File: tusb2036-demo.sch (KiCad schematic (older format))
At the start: 48 parts, among them J1 USB_B_Micro, J2 USB_A, J3 USB_A, J4 USB_A, SW1 RESET, U1 TUSB2036, U2 TPS76333, U3 TPS2044D, U4 SN75240, U5 SN75240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

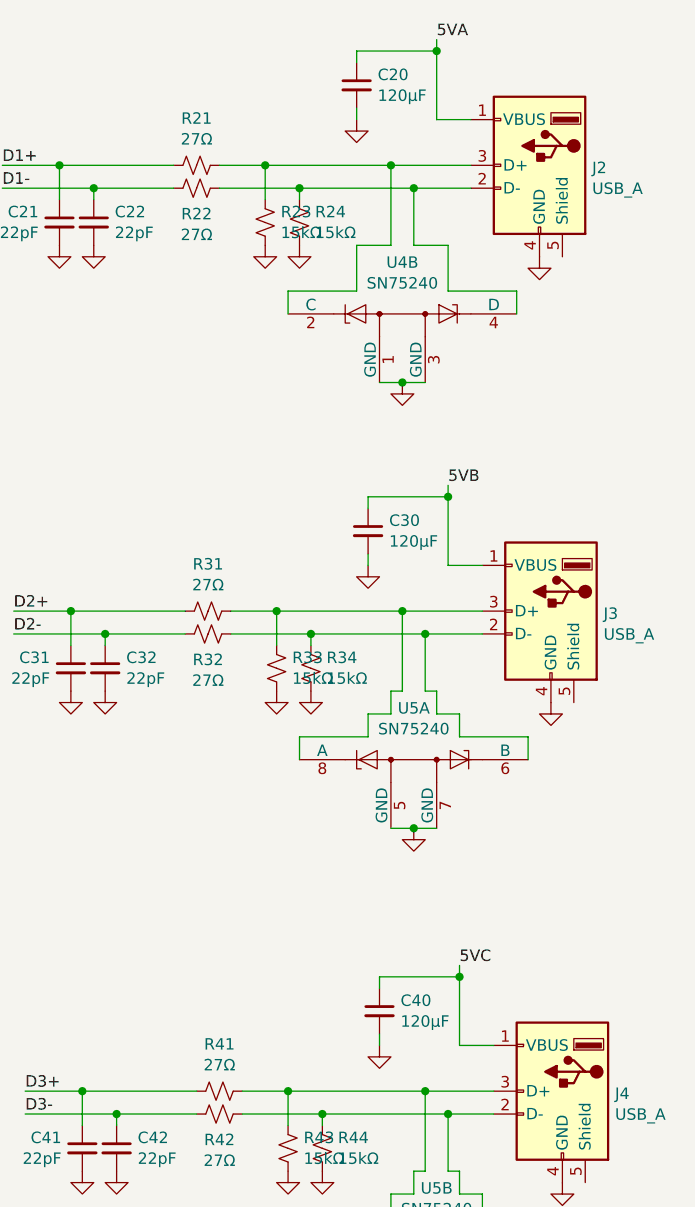
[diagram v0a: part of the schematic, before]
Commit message: Fix 120uF caps
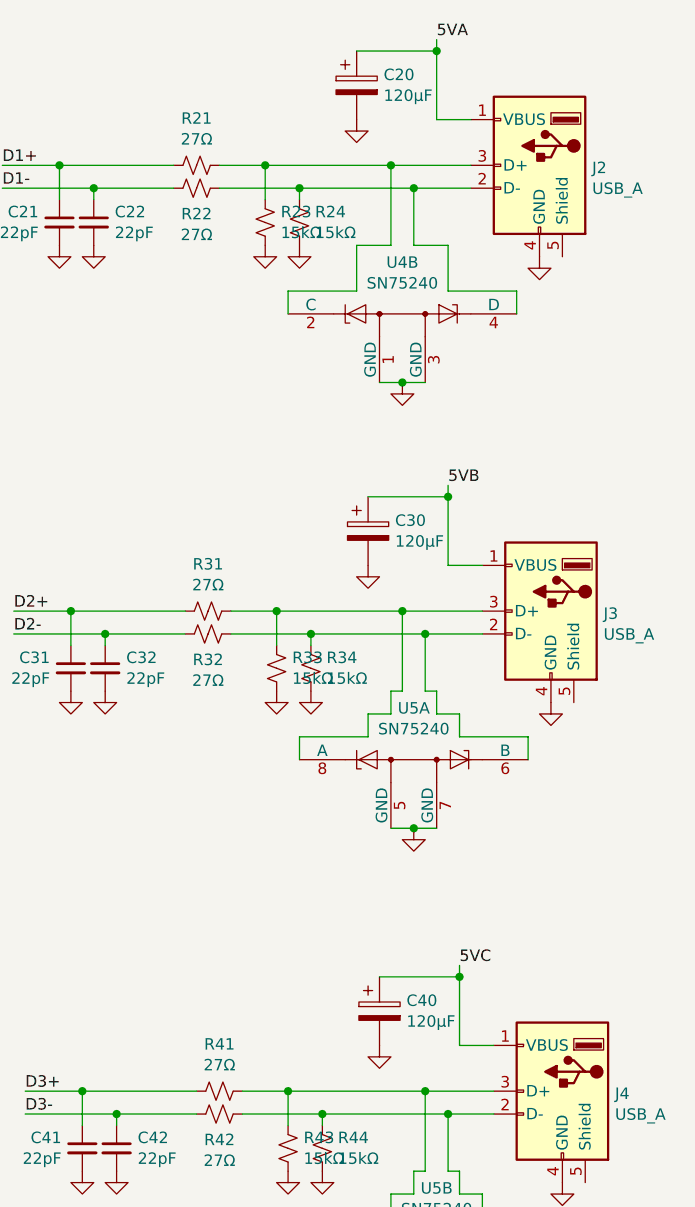
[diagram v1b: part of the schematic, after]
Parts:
- removed C20, C30, C40: 120μF, Capacitor_SMD:C_1206_3216Metric, symbol Device:C_Small
- added C20, C30, C40: 120μF, Vishay-cap:CAPPM7343X310N, symbol Device:CP
- C1, C10, C11, C2, C21, C22, C31, C32, C41, C42: Price (none) -> 0.61; Vendor (none) -> Mouser; Vendor Part # (none) -> 710-885012009007
- C3, C5: Price (none) -> 0.93; Vendor (none) -> Mouser; Vendor Part # (none) -> 80-C1210C475J3N
- C4: Price (none) -> 0.46; Vendor (none) -> Mouser; Vendor Part # (none) -> 581-12105C104JAT2A
- J3, J4: Price (none) -> 2.36; Vendor (none) -> Mouser; Vendor Part # (none) -> 710-62900416021
- JP1, JP2, JP3, JP4: Price (none) -> 0.1; Vendor (none) -> Mouser; Vendor Part # (none) -> 649-1012937890301BLF
- R1, R10, R11, R21, R22, R31, R32, R41, R42: Price (none) -> 0.14; Vendor (none) -> Mouser; Vendor Part # (none) -> 603-RC1210FR-0727RL
- R2: Price (none) -> 0.14; Vendor (none) -> Mouser; Vendor Part # (none) -> 603-RC1210FR-071K5L
- R23, R24, R33, R34, R43, R44: Price (none) -> 0.16; Vendor (none) -> Mouser; Vendor Part # (none) -> 603-RC1210FR-0715KL
- SW1: Price (none) -> 0.58; Vendor (none) -> Mouser; Vendor Part # (none) -> 653-B3FS-1002P
- TP1: Price (none) -> 0; Vendor (none) -> -; Vendor Part # (none) -> -
- U1: Price 3.40 -> 3.4
- U2: Price 1.00 -> 1
- U3: Price (none) -> 2.73; Vendor (none) -> Mouser; Vendor Part # (none) -> 595-TPS2044BDR
- U4, U5: Price (none) -> 1.31; Vendor (none) -> Mouser; Vendor Part # (none) -> 595-SN75240PWR
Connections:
- net 5VA: now also C20.1
- net 5VB: now also C30.1
- net 5VC: now also C40.1
- net GND: now also C20.2, C30.2, C40.2
